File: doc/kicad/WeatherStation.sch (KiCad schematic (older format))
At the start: 40 parts, among them J1 Conn_01x02, J10 Screw_Terminal_01x04, J11 Screw_Terminal_01x02, J12 Conn_01x02_Male, J13 Conn_01x02_Female, J14 Conn_01x02_Male, J15 Screw_Terminal_01x02, J16 Conn_01x02_Male, J17 Conn_01x02_Female, J18 Mess, J19 Prog, J2 Conn_01x04, J3 Screw_Terminal_01x02, J4 Conn_01x04_Male, J5 Conn_01x02_Male, J6 Conn_01x04_Male, J7 Conn_01x02_Male, J8 Screw_Terminal_01x04, J9 Screw_Terminal_01x02, Q1 IRLML2244, SW1 Reset, SW2 Mode, U1 BME280, U2 BH1750, U3 MPPT_StepDown, U4 Rain_Sensor, U5 LiIonCharger, U6 ESP-WROOM-32, U7 Mod_Spannungsteiler, U8 Mod_74LVC2G14GW, U9 Mod_MIC5501-3.0YM5-TR

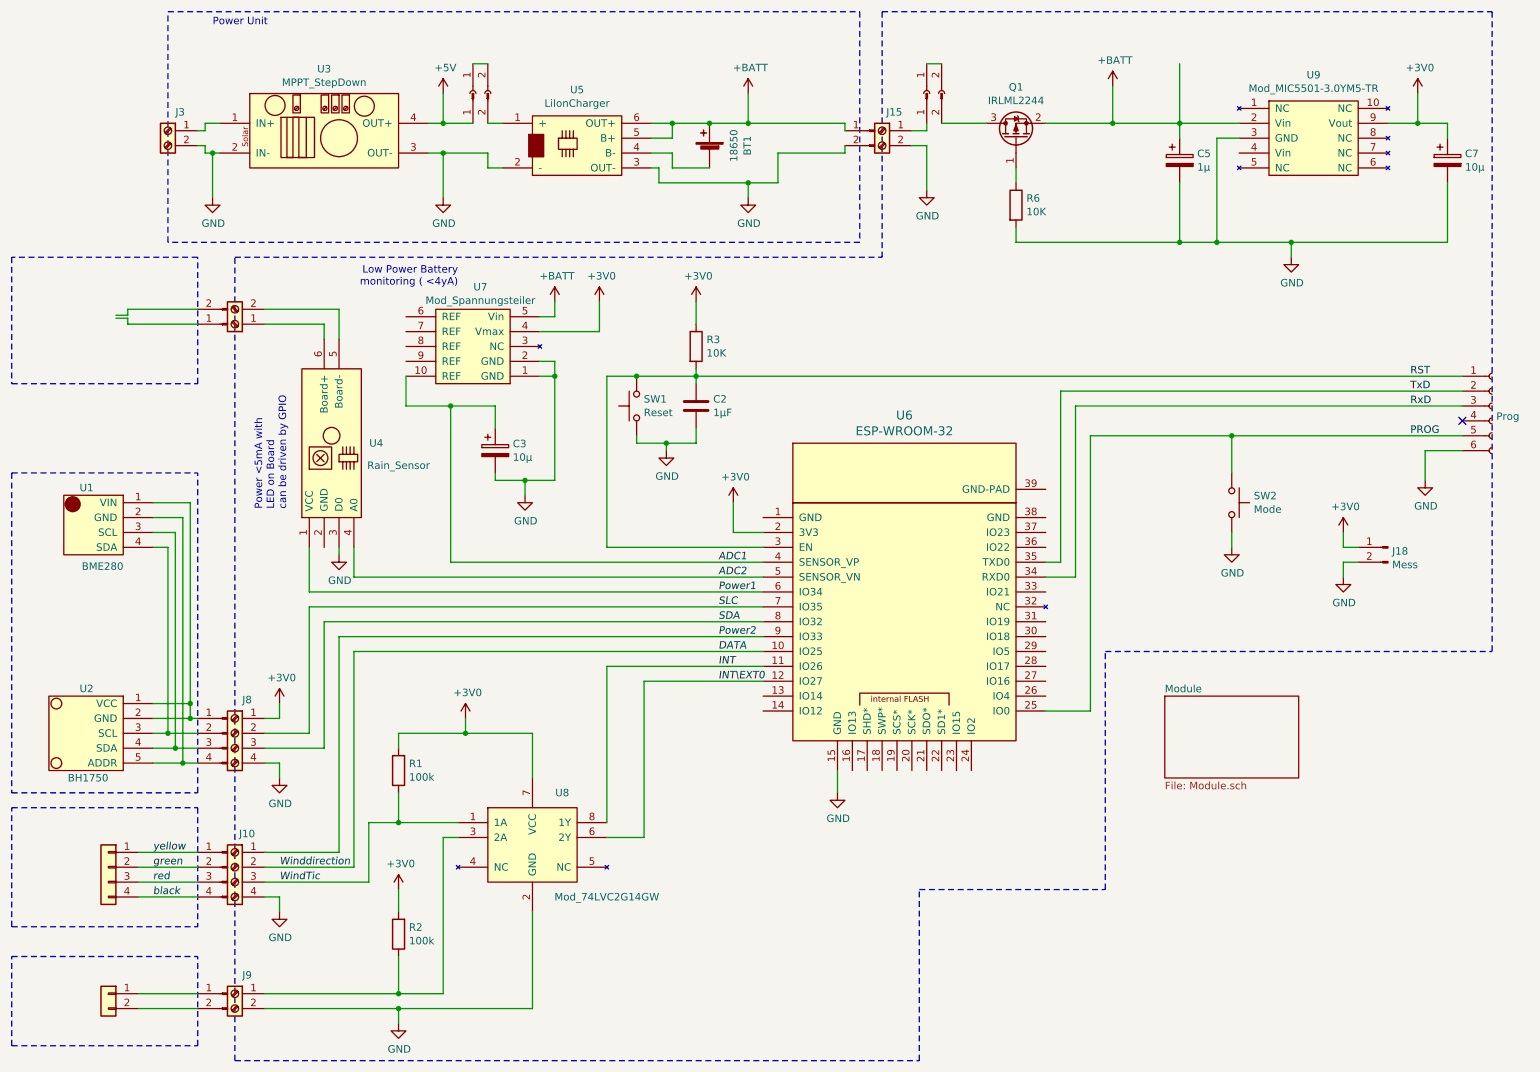
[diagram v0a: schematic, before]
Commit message: Stable without Solar monitor
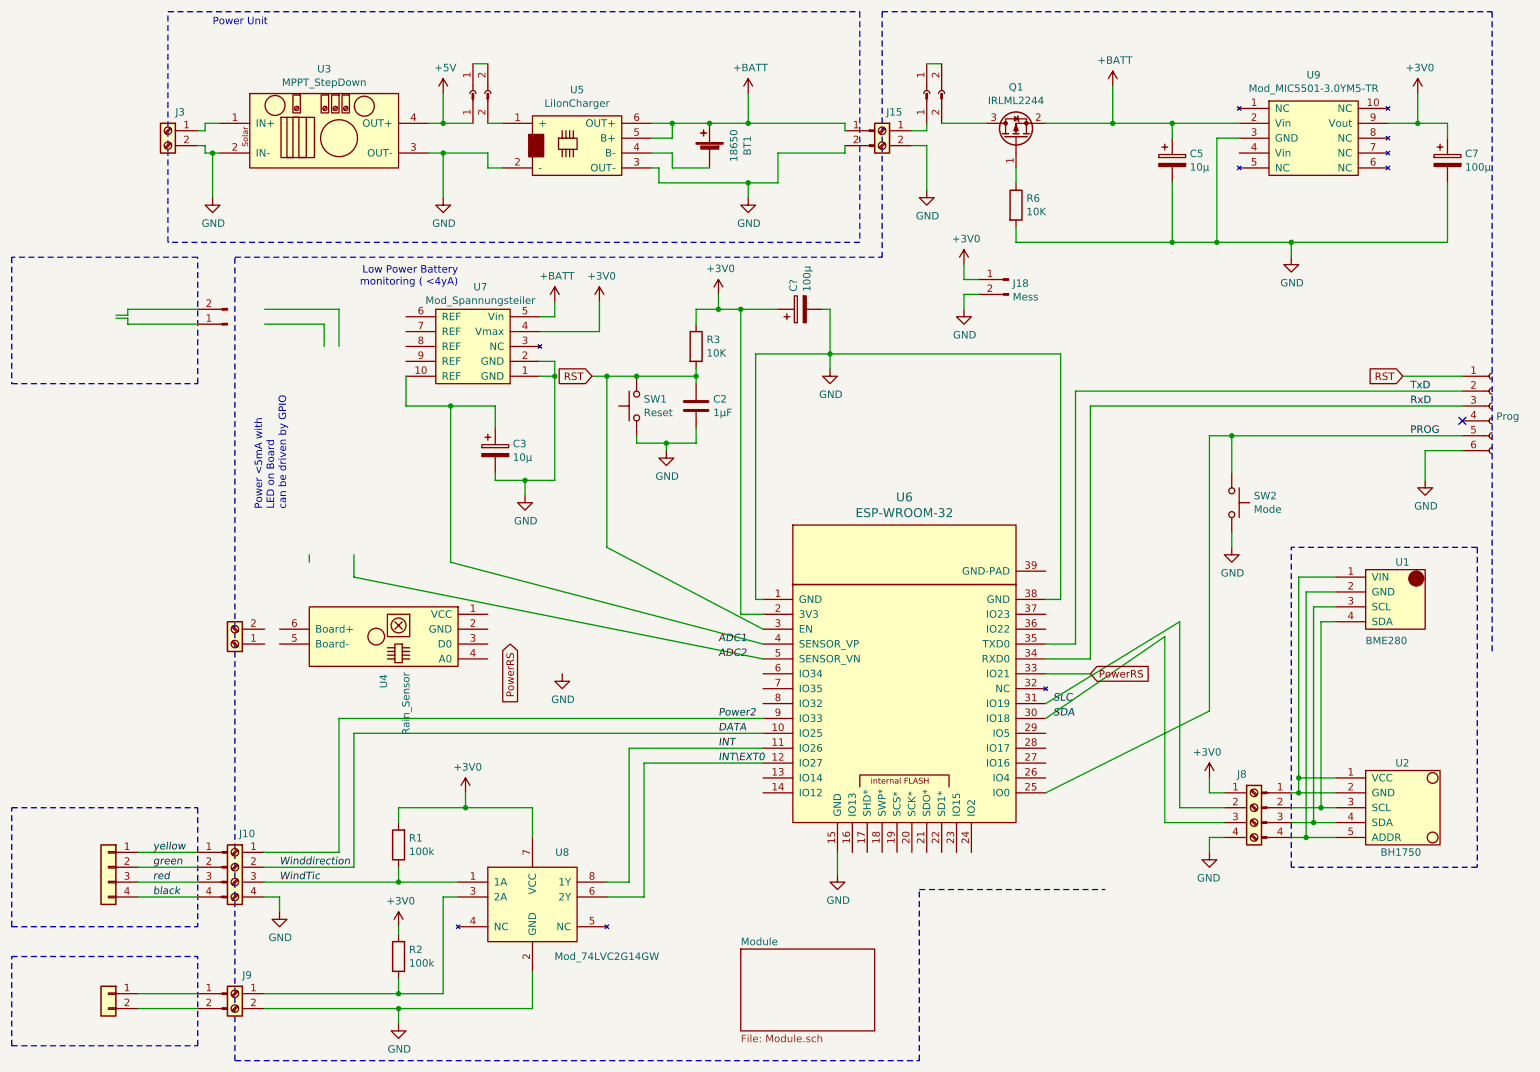
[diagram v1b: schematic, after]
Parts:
- added C?: 100µ, Capacitors_ThroughHole:CP_Radial_D4.0mm_P1.50mm, symbol Device:CP
- C5: value 1µ -> 10µ
- C7: value 10µ -> 100µ
- J19: footprint (none) -> Socket_Strips:Socket_Strip_Straight_1x06_Pitch2.54mm
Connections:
- net labels added: PowerRS
- net labels removed: Power1
- wire segments 198 -> 209
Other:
- moved on the sheet: C5, J18, J8, R1, R2, U1, U2, U4, U6, U8

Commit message: Fixed WiFi freeze (ADC_2/Int Problems). Optimize Solar MPPT.
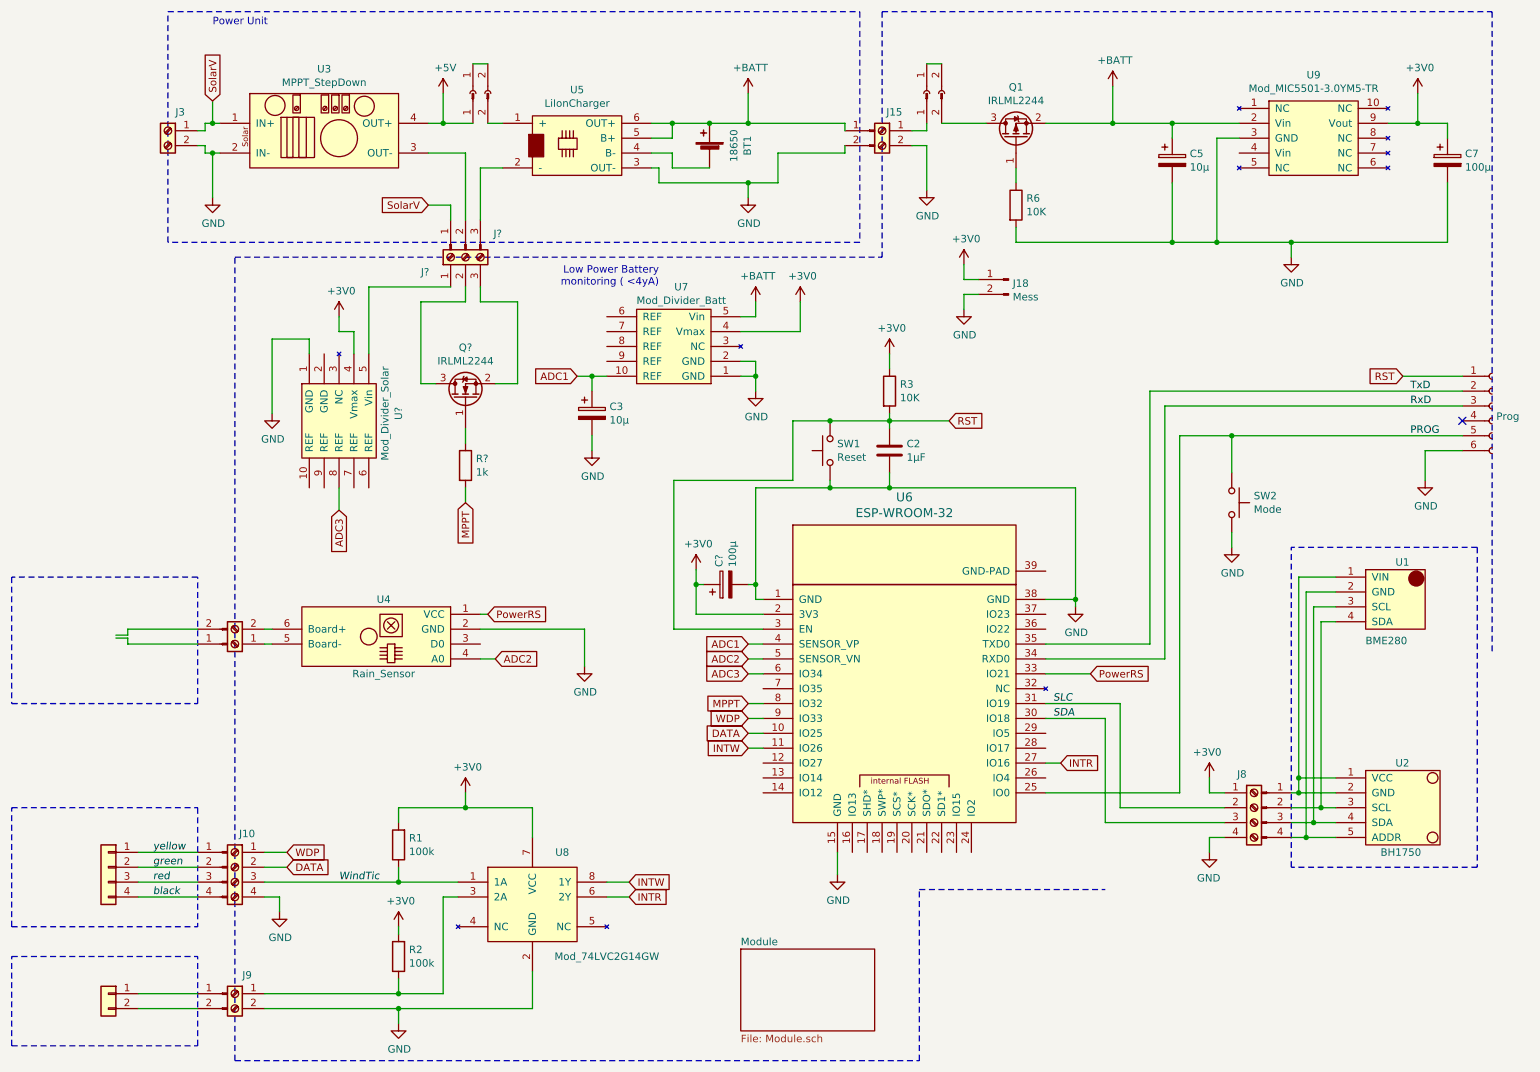
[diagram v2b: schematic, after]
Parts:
- added J?: Screw_Terminal_01x03, symbol Connector:Screw_Terminal_01x03
- added J?: Conn_01x03_Male, symbol Connector:Conn_01x03_Male
- added Q?: IRLML2244, Package_TO_SOT_SMD:SOT-23, symbol Transistor_FET:IRLML2060
- added R?: 1k, symbol Device:R
- added U?: Mod_Divider_Solar, Module:Mod_SOT23_TO_10DIL, symbol Module:Mod_Spannungsteiler
- U7: value Mod_Spannungsteiler -> Mod_Divider_Batt
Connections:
- net labels added: ADC3, INTR, INTW, MPPT, SolarV, WDP
- net labels removed: INT, INT\EXT0, Power2, Winddirection
- wire segments 209 -> 222
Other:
- note removed: "Power <5mA with\nLED on Board\ncan be driven by GPIO"
- moved on the sheet: C2, C3, C?, R3, SW1, U4, U7
